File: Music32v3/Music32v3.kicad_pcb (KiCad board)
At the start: 2 copper layers, 46 x 100 mm, 1 part

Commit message: Schematic
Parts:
- removed REF**: SRGP400200_ALPS, Music:SRGP400200_ALPS
- added BT1: Battery_Cell, Connector_JST:JST_GH_SM02B-GHS-TB_1x02-1MP_P1.25mm_Horizontal, F.Cu at (55.5, 71.5)
- added C1: 22uf, Capacitor_SMD:C_0805_2012Metric, F.Cu at (28.3, 63.1)
- added C10: 1uF, Capacitor_SMD:C_0402_1005Metric, F.Cu at (37.0, 57.2)
- added C11: 1uF, Capacitor_SMD:C_0402_1005Metric, F.Cu at (37.0, 59.7)
- added C12: 4.7uF, Capacitor_SMD:C_0402_1005Metric, F.Cu at (219.4, 63.7)
- added C13: 4.7uF, Capacitor_SMD:C_0402_1005Metric, F.Cu at (218.8, 67.7)
- added C14: 4.7uF, Capacitor_SMD:C_0402_1005Metric, F.Cu at (219.4, 65.6)
- added C15: 1uF, Capacitor_SMD:C_0402_1005Metric, F.Cu at (40.1, 20.7)
- added C16: 1uF, Capacitor_SMD:C_0402_1005Metric, F.Cu at (40.1, 23.2)
- added C17: 1uF, Capacitor_SMD:C_0402_1005Metric, F.Cu at (228.4, 56.8)
- added C18: 1uF, Capacitor_SMD:C_0402_1005Metric, F.Cu at (80.6, 10.8)
- added C19: 1uF, Capacitor_SMD:C_0402_1005Metric, F.Cu at (230.3, 55.8)
- added C2: 22uf, Capacitor_SMD:C_0805_2012Metric, F.Cu at (28.3, 66.2)
- added C20: 1uF, Capacitor_SMD:C_0402_1005Metric, F.Cu at (224.4, 55.7)
- added C21: 24pF, Capacitor_SMD:C_0402_1005Metric, F.Cu at (232.8, 52.1)
- added C22: 24pF, Capacitor_SMD:C_0402_1005Metric, F.Cu at (232.8, 56.8)
- added C23: 0.1uF, Capacitor_SMD:C_0402_1005Metric, F.Cu at (243.5, 65.5)
- added C24: 0.1uF, Capacitor_SMD:C_0402_1005Metric, F.Cu at (243.5, 68.0)
- added C25: 1uF, Capacitor_SMD:C_0402_1005Metric, F.Cu at (37.0, 62.2)
- added C26: 1uF, Capacitor_SMD:C_0402_1005Metric, F.Cu at (37.0, 64.7)
- added C27: 1uF, Capacitor_SMD:C_0402_1005Metric, F.Cu at (74.5, 52.2)
- added C28: 1uF, Capacitor_SMD:C_0402_1005Metric, F.Cu at (84.6, 5.78)
- added C29: 1uF, Capacitor_SMD:C_0402_1005Metric, F.Cu at (84.6, 8.29)
- added C3: 0.1uf, Capacitor_SMD:C_0402_1005Metric, F.Cu at (27.5, 68.6)
- added C30: 1uF, Capacitor_SMD:C_0402_1005Metric, F.Cu at (84.6, 10.8)
- added C31: 1uF, Capacitor_SMD:C_0402_1005Metric, F.Cu at (88.6, 0.76)
- added C32: 1uF, Capacitor_SMD:C_0402_1005Metric, F.Cu at (88.6, 3.27)
- added C33: 1uF, Capacitor_SMD:C_0402_1005Metric, F.Cu at (88.6, 5.78)
- added C34: 1uF, Capacitor_SMD:C_0402_1005Metric, F.Cu at (74.5, 54.7)
- added C35: 1uF, Capacitor_SMD:C_0402_1005Metric, F.Cu at (74.5, 57.2)
- added C36: 1uF, Capacitor_SMD:C_0402_1005Metric, F.Cu at (74.5, 59.7)
- added C37: 1uF, Capacitor_SMD:C_0402_1005Metric, F.Cu at (74.5, 62.2)
- added C38: 1uF, Capacitor_SMD:C_0402_1005Metric, F.Cu at (78.5, 52.2)
- added C39: 22uf, Capacitor_SMD:C_0805_2012Metric, F.Cu at (80.5, 70.1)
- added C4: 1uF, Capacitor_SMD:C_0402_1005Metric, F.Cu at (37.0, 52.2)
- added C40: 1uF, Capacitor_SMD:C_0402_1005Metric, F.Cu at (78.5, 54.7)
- added C41: 1uF, Capacitor_SMD:C_0402_1005Metric, F.Cu at (78.5, 57.2)
- added C42: 1uF, Capacitor_SMD:C_0402_1005Metric, F.Cu at (78.5, 59.7)
- added C43: 1uF, Capacitor_SMD:C_0402_1005Metric, F.Cu at (78.5, 62.2)
- added C44: 1uF, Capacitor_SMD:C_0402_1005Metric, F.Cu at (82.5, 52.2)
- added C45: 1uF, Capacitor_SMD:C_0402_1005Metric, F.Cu at (82.5, 54.7)
- added C46: 47nF, Capacitor_SMD:C_0402_1005Metric, F.Cu at (79.7, 72.6)
- added C47: 4.7uF, Capacitor_SMD:C_0402_1005Metric, F.Cu at (82.5, 57.2)
- added C48: 0.1uF, Capacitor_SMD:C_0402_1005Metric, F.Cu at (40.4, 77.8)
- added C5: 4.7uF, Capacitor_SMD:C_0402_1005Metric, F.Cu at (37.0, 54.7)
- added C6: 22uf, Capacitor_SMD:C_0805_2012Metric, F.Cu at (49.2, 69.3)
- added C7: 22uf, Capacitor_SMD:C_0805_2012Metric, F.Cu at (49.2, 72.3)
- added C8: 22uf, Capacitor_SMD:C_0805_2012Metric, F.Cu at (49.2, 75.3)
- added C9: 22uf, Capacitor_SMD:C_0805_2012Metric, F.Cu at (49.2, 78.3)
- added D1: LED_Small, LED_SMD:LED_0603_1608Metric, F.Cu at (43.9, 75.5)
- added D2: LED_Small, LED_SMD:LED_0603_1608Metric, F.Cu at (43.9, 78.1)
- added D3: LED, LED_SMD:LED_0603_1608Metric, F.Cu at (209.0, 69.6)
- added D4: DSS34, Diode_SMD:D_SOD-123F, F.Cu at (54.2, 76.9)
- added F1: Polyfuse, Fuse:Fuse_0603_1608Metric, F.Cu at (37.0, 67.2)
- added F2: Polyfuse, Fuse:Fuse_0603_1608Metric, F.Cu at (37.0, 69.7)
- added FB1: 100ohm@100MHz, Resistor_SMD:R_0402_1005Metric, F.Cu at (216.8, 67.7)
- added J1: USB_C_Receptacle_USB2.0, Music:U263-163N-4OS1735, F.Cu at (226.3, 39.1)
- added J2: PJ-316A-6A, Music:PJ-316A-6A, F.Cu at (67.0, 51.7)
- added J3: Micro_SD_Card_Det1, Music:MOLEX_503398-1892, F.Cu at (193.6, 79.4)
- added MK1: GMI4015P-2C-66db, Music:GMI4015P-2C-66db, F.Cu at (80.9, 66.0)
- added Q1: CJ3134K KF, Package_TO_SOT_SMD:SOT-723, F.Cu at (52.1, 52.3)
- added Q2: CJ3134K KF, Package_TO_SOT_SMD:SOT-723, F.Cu at (52.1, 55.2)
- added Q3: YJQD30P02A, Music:YJQD30P02A_DFN3.3x3.3, F.Cu at (55.9, 53.5)
- added Q4: CJ3139K, Package_TO_SOT_SMD:SOT-723, F.Cu at (80.0, 13.5)
- added Q5: CJ3134K KF, Package_TO_SOT_SMD:SOT-723, F.Cu at (238.8, 71.2)
- added Q6: CJ3134K KF, Package_TO_SOT_SMD:SOT-723, F.Cu at (240.9, 71.2)
- added Q7: CJ3134K KF, Package_TO_SOT_SMD:SOT-723, F.Cu at (47.8, 20.8)
- added R1: 10k, Resistor_SMD:R_0402_1005Metric, F.Cu at (19.4, 79.0)
- added R10: 10R, Resistor_SMD:R_0402_1005Metric, F.Cu at (36.7, 20.4)
- added R11: 1M, Resistor_SMD:R_0402_1005Metric, F.Cu at (36.7, 22.4)
- added R12: 1M, Resistor_SMD:R_0402_1005Metric, F.Cu at (40.4, 73.8)
- added R13: 1M, Resistor_SMD:R_0402_1005Metric, F.Cu at (40.4, 75.8)
- added R14: 1M, Resistor_SMD:R_0402_1005Metric, F.Cu at (67.9, 16.7)
- added R15: 1M, Resistor_SMD:R_0402_1005Metric, F.Cu at (19.4, 81.0)
- added R16: DNP, Resistor_SMD:R_0402_1005Metric, F.Cu at (67.9, 18.7)
- added R17: DNP, Resistor_SMD:R_0402_1005Metric, F.Cu at (67.9, 20.7)
- added R18: DNP, Resistor_SMD:R_0402_1005Metric, F.Cu at (70.8, 16.7)
- added R19: 4K7, Resistor_SMD:R_0402_1005Metric, F.Cu at (240.9, 69.6)
- added R2: 1M, Resistor_SMD:R_0402_1005Metric, F.Cu at (40.4, 61.9)
- added R20: DNP, Resistor_SMD:R_0402_1005Metric, F.Cu at (238.8, 69.6)
- added R21: 2K, Resistor_SMD:R_0402_1005Metric, F.Cu at (19.4, 83.0)
- added R22: 2K, Resistor_SMD:R_0402_1005Metric, F.Cu at (19.4, 84.9)
- added R23: 10K, Resistor_SMD:R_0402_1005Metric, F.Cu at (73.9, 64.5)
- added R24: 0R, Resistor_SMD:R_0402_1005Metric, F.Cu at (73.9, 66.5)
- added R25: 10K, Resistor_SMD:R_0402_1005Metric, F.Cu at (73.9, 68.4)
- added R26: 220R, Resistor_SMD:R_0402_1005Metric, F.Cu at (73.9, 70.4)
- added R27: 220R, Resistor_SMD:R_0402_1005Metric, F.Cu at (73.9, 72.4)
- added R28: 1M, Resistor_SMD:R_0402_1005Metric, F.Cu at (73.9, 74.4)
- added R29: 10K, Resistor_SMD:R_0402_1005Metric, F.Cu at (76.8, 64.5)
- added R3: 5.1K, Resistor_SMD:R_0402_1005Metric, F.Cu at (40.4, 63.9)
- added R30: 2K, Resistor_SMD:R_0402_1005Metric, F.Cu at (76.8, 66.5)
- added R31: 2K, Resistor_SMD:R_0402_1005Metric, F.Cu at (76.8, 68.4)
- added R32: 33R, Resistor_SMD:R_0402_1005Metric, F.Cu at (76.8, 70.4)
- added R33: 33R, Resistor_SMD:R_0402_1005Metric, F.Cu at (76.8, 72.4)
- added R34: 1M, Resistor_SMD:R_0402_1005Metric, F.Cu at (36.7, 24.4)
- added R35: 2K, Resistor_SMD:R_0402_1005Metric, F.Cu at (22.3, 79.0)
- added R36: 10K, Resistor_SMD:R_0402_1005Metric, F.Cu at (22.3, 81.0)
- added R37: 2K, Resistor_SMD:R_0402_1005Metric, F.Cu at (22.3, 83.0)
- added R38: 2K, Resistor_SMD:R_0402_1005Metric, F.Cu at (22.3, 84.9)
- added R39: 2K, Resistor_SMD:R_0402_1005Metric, F.Cu at (25.2, 79.0)
- added R4: 5.1K, Resistor_SMD:R_0402_1005Metric, F.Cu at (40.4, 65.9)
- added R40: 2K, Resistor_SMD:R_0402_1005Metric, F.Cu at (25.2, 81.0)
- added R41: 10K, Resistor_SMD:R_0402_1005Metric, F.Cu at (25.2, 83.0)
- added R42: 10K, Resistor_SMD:R_0402_1005Metric, F.Cu at (25.2, 84.9)
- added R43: 2K, Resistor_SMD:R_0402_1005Metric, F.Cu at (28.1, 79.0)
- added R44: 10K, Resistor_SMD:R_0402_1005Metric, F.Cu at (28.1, 81.0)
- added R45: 1M, Resistor_SMD:R_0402_1005Metric, F.Cu at (36.7, 26.4)
- added R46: 1M, Resistor_SMD:R_0402_1005Metric, F.Cu at (36.7, 28.4)
- added R47: 1M, Resistor_SMD:R_0402_1005Metric, F.Cu at (36.7, 30.4)
- added R48: 1M, Resistor_SMD:R_0402_1005Metric, F.Cu at (28.1, 83.0)
- added R49: 1M, Resistor_SMD:R_0402_1005Metric, F.Cu at (28.1, 84.9)
- added R5: 2K, Resistor_SMD:R_0402_1005Metric, F.Cu at (40.4, 67.9)
- added R6: 2K, Resistor_SMD:R_0402_1005Metric, F.Cu at (40.4, 69.9)
- added R7: 2K, Resistor_SMD:R_0402_1005Metric, F.Cu at (40.4, 71.8)
- added R8: 2K, Resistor_SMD:R_0402_1005Metric, F.Cu at (211.6, 69.6)
- added R9: 100K, Resistor_SMD:R_0402_1005Metric, F.Cu at (65.0, 20.7)
- added SW1: RESET, Music:TS3315A, F.Cu at (2.77, 53.4)
- added SW2: Power, Button_Switch_SMD:SW_SPDT_PCM12, F.Cu at (51.9, 63.9)
- added SW3: PP, Music:TS3315A, F.Cu at (2.77, 58.5)
- added SW4: RW, Music:TS3315A, F.Cu at (2.77, 63.5)
- added SW5: FF, Music:TS3315A, F.Cu at (2.77, 68.6)
- added SW6: HOME, Music:TS3315A, F.Cu at (2.77, 73.6)
- added SW7: Vol+, Music:TSA002A3816B04, F.Cu at (29.5, 53.9)
- added SW8: Vol+, Music:TSA002A3816B04, F.Cu at (29.5, 59.2)
- added SW9: Select, Music:TS3315A, F.Cu at (2.77, 78.7)
- added U1: ESP32-WROOM-32E__16MB_, Music:ESP32-WROOM-32E, F.Cu at (16.1, 67.2)
- added U10: TPD2EUSB30, Package_TO_SOT_SMD:Texas_DRT-3, F.Cu at (202.5, 76.4)
- added U11: TPD2EUSB30, Package_TO_SOT_SMD:Texas_DRT-3, F.Cu at (202.5, 78.8)
- added U12: TPD2EUSB30, Package_TO_SOT_SMD:Texas_DRT-3, F.Cu at (202.5, 80.8)
- added U13: SN74LVC1G3157, Package_TO_SOT_SMD:SOT-363_SC-70-6, F.Cu at (212.1, 75.7)
- added U14: SN74LVC1G3157, Package_TO_SOT_SMD:SOT-363_SC-70-6, F.Cu at (212.1, 79.5)
- added U15: SN74LVC1G3157, Package_TO_SOT_SMD:SOT-363_SC-70-6, F.Cu at (212.1, 83.3)
- added U16: SN74LVC1G3157, Package_TO_SOT_SMD:SOT-363_SC-70-6, F.Cu at (212.1, 87.2)
- added U17: SN74LVC1G3157, Package_TO_SOT_SMD:SOT-363_SC-70-6, F.Cu at (212.1, 91.0)
- added U18: CH340X, Package_SO:MSOP-10_3x3mm_P0.5mm, F.Cu at (239.8, 67.0)
- added U19: SN74LVC1G3157, Package_TO_SOT_SMD:SOT-363_SC-70-6, F.Cu at (212.1, 94.9)
- added U2: XC6210B332MR, Package_TO_SOT_SMD:SOT-23-5, F.Cu at (44.4, 63.1)
- added U20: SSP61CC3602MR, Package_TO_SOT_SMD:SOT-23-3, F.Cu at (44.4, 72.0)
- added U21: ES8327, Package_DFN_QFN:QFN-32-1EP_4x4mm_P0.4mm_EP2.9x2.9mm_ThermalVias, F.Cu at (64.6, 67.6)
- added U22: SRGP400200, Music:SRGP400200_ALPS, F.Cu at (46.9, 8.73)
- added U23: Sk-3393, Music:SK-3393M-G1, F.Cu at (12.0, 81.0)
- added U3: SSP6206-18NR, Package_TO_SOT_SMD:SOT-23, F.Cu at (55.9, 58.1)
- added U4: TPD2EUSB30, Package_TO_SOT_SMD:Texas_DRT-3, F.Cu at (226.3, 45.0)
- added U5: TP4057, Package_TO_SOT_SMD:SOT-23-6, F.Cu at (44.4, 67.6)
- added U6: GL823, Package_SO:SSOP-16_3.9x4.9mm_P0.635mm, F.Cu at (215.4, 64.3)
- added U7: ~, Music:SL2.1S, F.Cu at (227.3, 53.7)
- added U8: ST7889 2" LCD, Music:TFT020-2_same_side, F.Cu at (18.9, 25.7)
- added U9: MAX17048, Package_DFN_QFN:DFN-8-1EP_2x2mm_P0.5mm_EP0.8x1.6mm, F.Cu at (44.3, 21.2)
- added Y1: 12MHz, Crystal:Crystal_SMD_2520-4Pin_2.5x2.0mm, F.Cu at (232.8, 54.5)

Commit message: PCB outline
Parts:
- removed BT1: Battery_Cell, Connector_JST:JST_GH_SM02B-GHS-TB_1x02-1MP_P1.25mm_Horizontal
- removed C1, C2, C39, C6, C7, C8, C9: 22uf, Capacitor_SMD:C_0805_2012Metric
- removed C10, C11, C15, C16, C17, C18, C19, C20, C25, C26, C27, C28, C29, C30, C31, C32, C33, C34, C35, C36, C37, C38, C4, C40, C41, C42, C43, C44, C45: 1uF, Capacitor_SMD:C_0402_1005Metric
- removed C12, C13, C14, C47, C5: 4.7uF, Capacitor_SMD:C_0402_1005Metric
- removed C21, C22: 24pF, Capacitor_SMD:C_0402_1005Metric
- removed C23, C24, C48: 0.1uF, Capacitor_SMD:C_0402_1005Metric
- removed C3: 0.1uf, Capacitor_SMD:C_0402_1005Metric
- removed C46: 47nF, Capacitor_SMD:C_0402_1005Metric
- removed D1, D2: LED_Small, LED_SMD:LED_0603_1608Metric
- removed D3: LED, LED_SMD:LED_0603_1608Metric
- removed D4: DSS34, Diode_SMD:D_SOD-123F
- removed F1, F2: Polyfuse, Fuse:Fuse_0603_1608Metric
- removed FB1: 100ohm@100MHz, Resistor_SMD:R_0402_1005Metric
- removed J3: Micro_SD_Card_Det1, Music:MOLEX_503398-1892
- removed Q1, Q2, Q5, Q6, Q7: CJ3134K KF, Package_TO_SOT_SMD:SOT-723
- removed Q3: YJQD30P02A, Music:YJQD30P02A_DFN3.3x3.3
- removed Q4: CJ3139K, Package_TO_SOT_SMD:SOT-723
- removed R1: 10k, Resistor_SMD:R_0402_1005Metric
- removed R10: 10R, Resistor_SMD:R_0402_1005Metric
- removed R11, R12, R13, R14, R15, R2, R28, R34, R45, R46, R47, R48, R49: 1M, Resistor_SMD:R_0402_1005Metric
- removed R16, R17, R18, R20: DNP, Resistor_SMD:R_0402_1005Metric
- removed R19: 4K7, Resistor_SMD:R_0402_1005Metric
- removed R21, R22, R30, R31, R35, R37, R38, R39, R40, R43, R5, R6, R7, R8: 2K, Resistor_SMD:R_0402_1005Metric
- removed R23, R25, R29, R36, R41, R42, R44: 10K, Resistor_SMD:R_0402_1005Metric
- removed R24: 0R, Resistor_SMD:R_0402_1005Metric
- removed R26, R27: 220R, Resistor_SMD:R_0402_1005Metric
- removed R3, R4: 5.1K, Resistor_SMD:R_0402_1005Metric
- removed R32, R33: 33R, Resistor_SMD:R_0402_1005Metric
- removed R9: 100K, Resistor_SMD:R_0402_1005Metric
- removed SW1: RESET, Music:TS3315A
- removed SW2: Power, Button_Switch_SMD:SW_SPDT_PCM12
- removed U1: ESP32-WROOM-32E__16MB_, Music:ESP32-WROOM-32E
- removed U10, U11, U12, U4: TPD2EUSB30, Package_TO_SOT_SMD:Texas_DRT-3
- removed U13, U14, U15, U16, U17, U19: SN74LVC1G3157, Package_TO_SOT_SMD:SOT-363_SC-70-6
- removed U18: CH340X, Package_SO:MSOP-10_3x3mm_P0.5mm
- removed U2: XC6210B332MR, Package_TO_SOT_SMD:SOT-23-5
- removed U20: SSP61CC3602MR, Package_TO_SOT_SMD:SOT-23-3
- removed U21: ES8327, Package_DFN_QFN:QFN-32-1EP_4x4mm_P0.4mm_EP2.9x2.9mm_ThermalVias
- removed U23: Sk-3393, Music:SK-3393M-G1
- removed U3: SSP6206-18NR, Package_TO_SOT_SMD:SOT-23
- removed U5: TP4057, Package_TO_SOT_SMD:SOT-23-6
- removed U6: GL823, Package_SO:SSOP-16_3.9x4.9mm_P0.635mm
- removed U7: ~, Music:SL2.1S
- removed U9: MAX17048, Package_DFN_QFN:DFN-8-1EP_2x2mm_P0.5mm_EP0.8x1.6mm
- removed Y1: 12MHz, Crystal:Crystal_SMD_2520-4Pin_2.5x2.0mm
- MK1, SW9, U22, U8: moved to B.Cu
- SW3: value PP -> Vol+; footprint Music:TS3315A -> Music:TSA002A3816B04
- SW4: value RW -> Vol+; footprint Music:TS3315A -> Music:TSA002A3816B04
- SW5: value FF -> PP; moved to B.Cu
- SW6: value HOME -> RW; moved to B.Cu
- SW7: value Vol+ -> FF; footprint Music:TSA002A3816B04 -> Music:TS3315A; moved to B.Cu
- SW8: value Vol+ -> HOME; footprint Music:TSA002A3816B04 -> Music:TS3315A; moved to B.Cu
- moved SW6 150.6 mm to (144.0, 126.0), turned to -90 degrees
- moved SW5 145.9 mm to (130.0, 140.0), turned to 180 degrees
- moved J1 145.0 mm to (130.0, 147.4), turned to 0 degrees
- moved U22 143.7 mm to (130.0, 126.0), turned to 90 degrees
- moved SW9 135.7 mm to (130.0, 126.0), turned to -90 degrees
- moved U8 123.1 mm to (128.5, 81.7), turned to 180 degrees
- moved SW8 113.5 mm to (130.0, 112.0), turned to 180 degrees
- moved SW7 112.6 mm to (116.0, 126.0), turned to -90 degrees
- moved SW4 111.4 mm to (111.8, 86.4), turned to 90 degrees
- moved SW3 109.9 mm to (111.8, 72.4), turned to 90 degrees
- moved J2 70.5 mm to (137.5, 50.0)
- moved MK1 65.0 mm to (144.7, 53.7), turned to 180 degrees
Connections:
- SW3 pad 2: +3.3V -> +3V3
- SW4 pad 2: +3.3V -> +3V3
- SW5 pad 2: +3.3V -> +3V3
- SW6 pad 1: BUTTONS -> Net-(R41-Pad1)
- SW6 pad 2: +3.3V -> +3V3
- SW7 pad 2: +3.3V -> +3V3
- SW8 pad 1: Net-(R44-Pad2) -> BUTTONS
- SW8 pad 2: +3.3V -> +3V3
- U8 pad 4: +3.3V -> +3V3
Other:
- outline, holes or cut-outs redrawn

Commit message: Board setup
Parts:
- added J2: Micro_SD_Card_Det1, Music:MOLEX_503398-1892, F.Cu at (114.9, 106.5)
- added SW9: Power, Button_Switch_SMD:SW_SPDT_PCM12, F.Cu at (111.0, 121.2)
- added U3: Sk-3393, Music:SK-3393M-G1, F.Cu at (146.5, 71.9)
- added U5: ESP32-WROOM-32E__16MB_, Music:ESP32-WROOM-32E, F.Cu at (137.2, 108.9)
- SW3: renamed from SW4; value Vol+ -> Vol-
- moved J3 7.50 mm to (130.0, 50.0)
- moved SW1 1.70 mm to (113.5, 72.4)
- moved SW3 1.70 mm to (113.5, 86.4)
- turned MK1 to 0 degrees
- turned SW6 to 90 degrees
- turned SW7 to 0 degrees
- renumbered J2 to J3, SW3 to SW1, SW9 to SW2, SW5 to SW4, SW6 to SW5, SW7 to SW6, SW8 to SW7, U8 to U1, U22 to U4
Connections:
- U1 pad 9: CLK -> CLK_UC
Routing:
- net GND: vias 0 -> 16
- added copper zone on B.Cu, net GND
- added copper zone on F.Cu, net GND
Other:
- outline, holes or cut-outs redrawn
- copper layers 2 -> 4

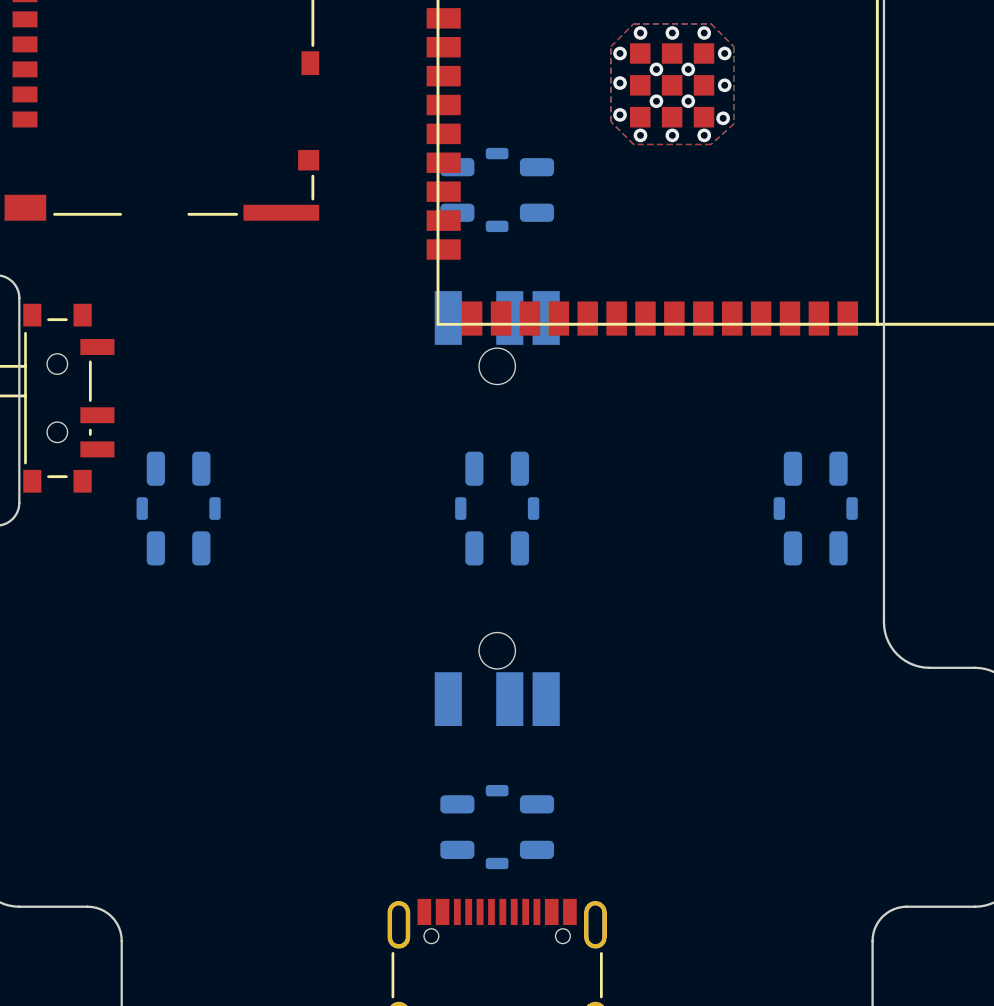
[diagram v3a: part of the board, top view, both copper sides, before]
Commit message: Button placement fix
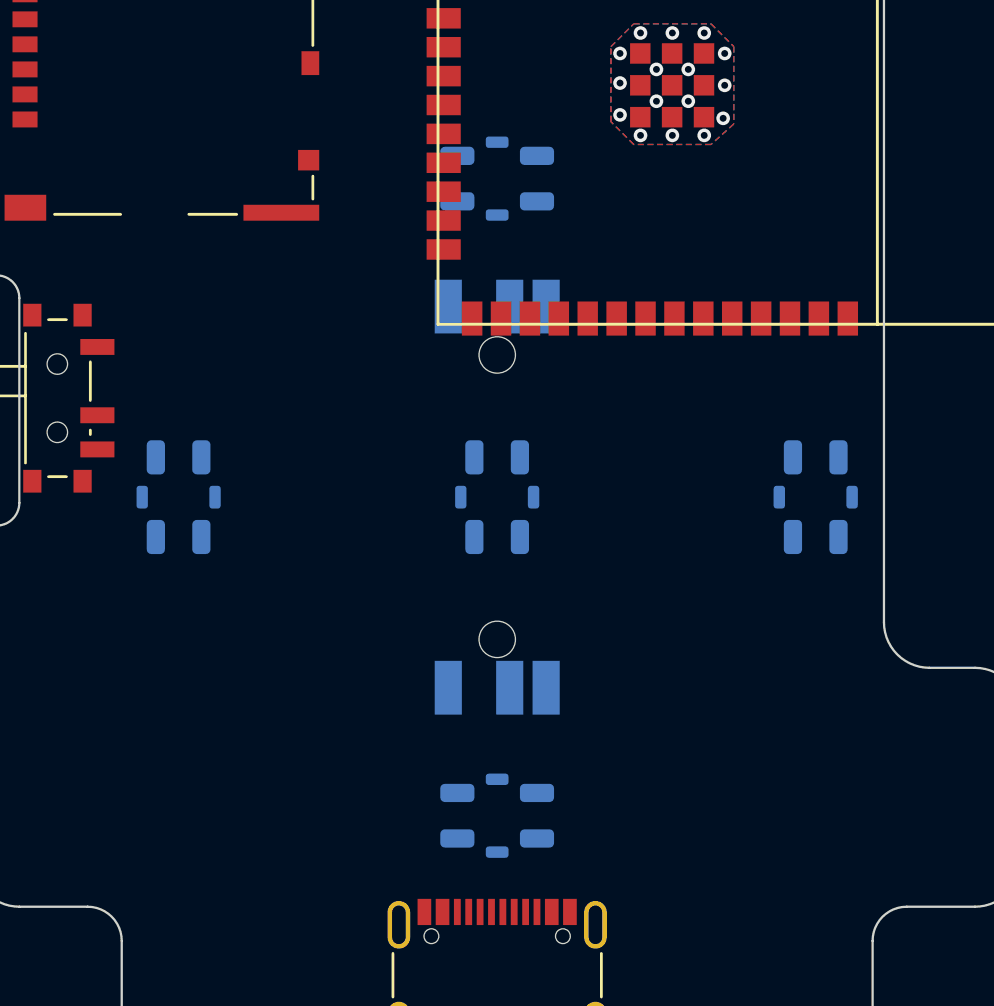
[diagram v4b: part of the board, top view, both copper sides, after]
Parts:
- moved SW2 0.50 mm to (130.0, 125.5)
- moved SW4 0.50 mm to (130.0, 139.5)
- moved SW5 0.50 mm to (144.0, 125.5)
- moved SW6 0.50 mm to (116.0, 125.5)
- moved SW7 0.50 mm to (130.0, 111.5)
- moved U4 0.50 mm to (130.0, 125.5)
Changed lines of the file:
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@@
   )
   (footprint "Music:TS3315A" locked (layer "B.Cu")
-    (at 144 126 -90)
+    (at 144 125.5 -90)
     (property "Sheetfile" "Music32v3.kicad_sch")
     (property "Sheetname" "")
@@
   )
   (footprint "Music:TS3315A" locked (layer "B.Cu")
-    (at 130 126 -90)
+    (at 130 125.5 -90)
     (property "Sheetfile" "Music32v3.kicad_sch")
     (property "Sheetname" "")
@@
   )
   (footprint "Music:TS3315A" locked (layer "B.Cu")
-    (at 130 140 180)
+    (at 130 139.5 180)
     (property "Sheetfile" "Music32v3.kicad_sch")
     (property "Sheetname" "")
@@
   )
   (footprint "Music:TS3315A" locked (layer "B.Cu")
-    (at 116 126 90)
+    (at 116 125.5 90)
     (property "Sheetfile" "Music32v3.kicad_sch")
     (property "Sheetname" "")
@@
   )
   (footprint "Music:SRGP400200_ALPS" locked (layer "B.Cu")
-    (at 130 126 90)
+    (at 130 125.5 90)
     (tags "SRGP400200 ")
     (property "Sheetfile" "Music32v3.kicad_sch")
@@
   )
   (footprint "Music:TS3315A" locked (layer "B.Cu")
-    (at 130 112)
+    (at 130 111.5)
     (property "Sheetfile" "Music32v3.kicad_sch")
     (property "Sheetname" "")
@@
     )
   )
-  (gr_circle locked (center 130 126) (end 111 126)
+  (gr_circle locked (center 130 125.5) (end 111 125.5)
     (stroke (width 0.1) (type default)) (fill none) (layer "B.SilkS"))
-  (gr_circle locked (center 130 126) (end 121 126)
+  (gr_circle locked (center 130 125.5) (end 121 125.5)
     (stroke (width 0.1) (type default)) (fill none) (layer "B.SilkS"))
-  (gr_circle locked (center 130 126) (end 123 126)
+  (gr_circle locked (center 130 125.5) (end 123 125.5)
     (stroke (width 0.1) (type default)) (fill none) (layer "B.SilkS"))
   (gr_line locked (start 111 93.5) (end 108 93.5)
